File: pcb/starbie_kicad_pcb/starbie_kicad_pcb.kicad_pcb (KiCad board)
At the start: 2 copper layers, 7 parts, among them J1 Conn_01x04_Pin, J2 Conn_01x08_Pin, SW1 SW_Push, SW2 SW_Push, U1 DHT11, U2 XIAO-ESP32-C3-SMD

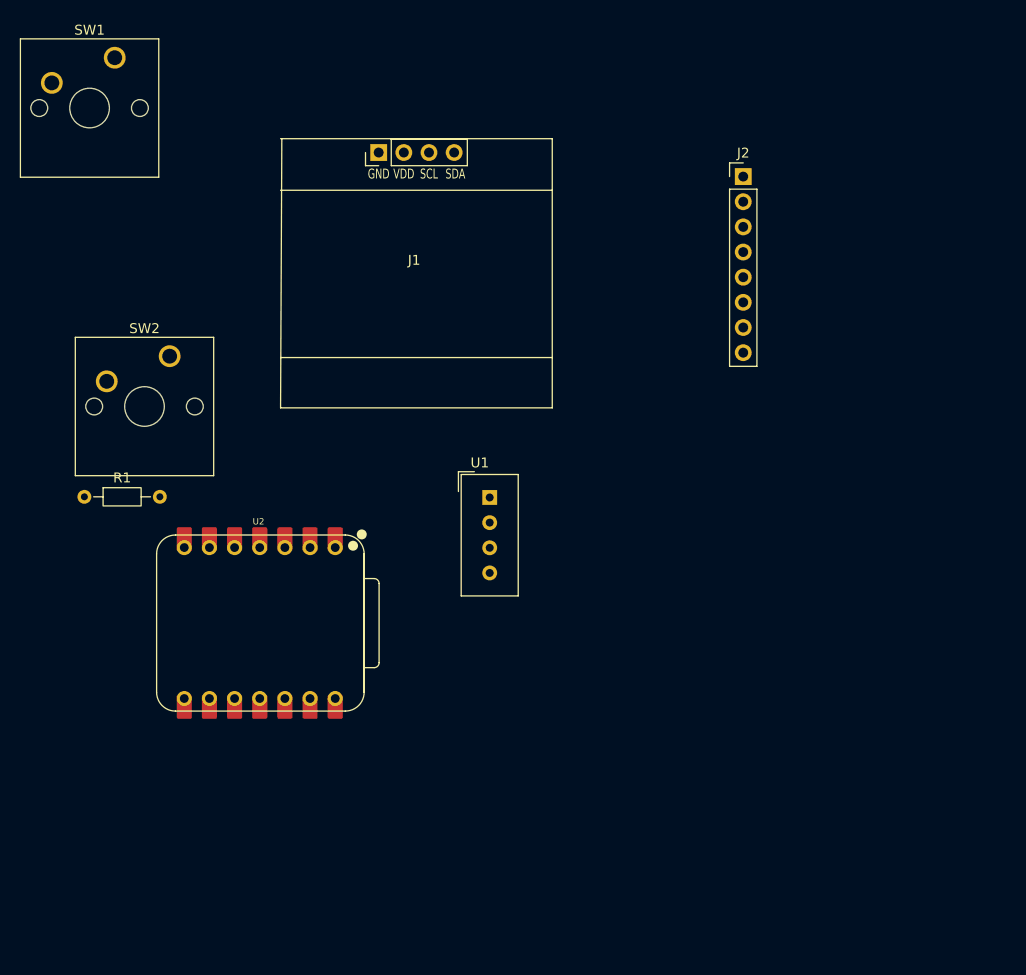
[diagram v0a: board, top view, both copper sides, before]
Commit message: added arduino sketch files
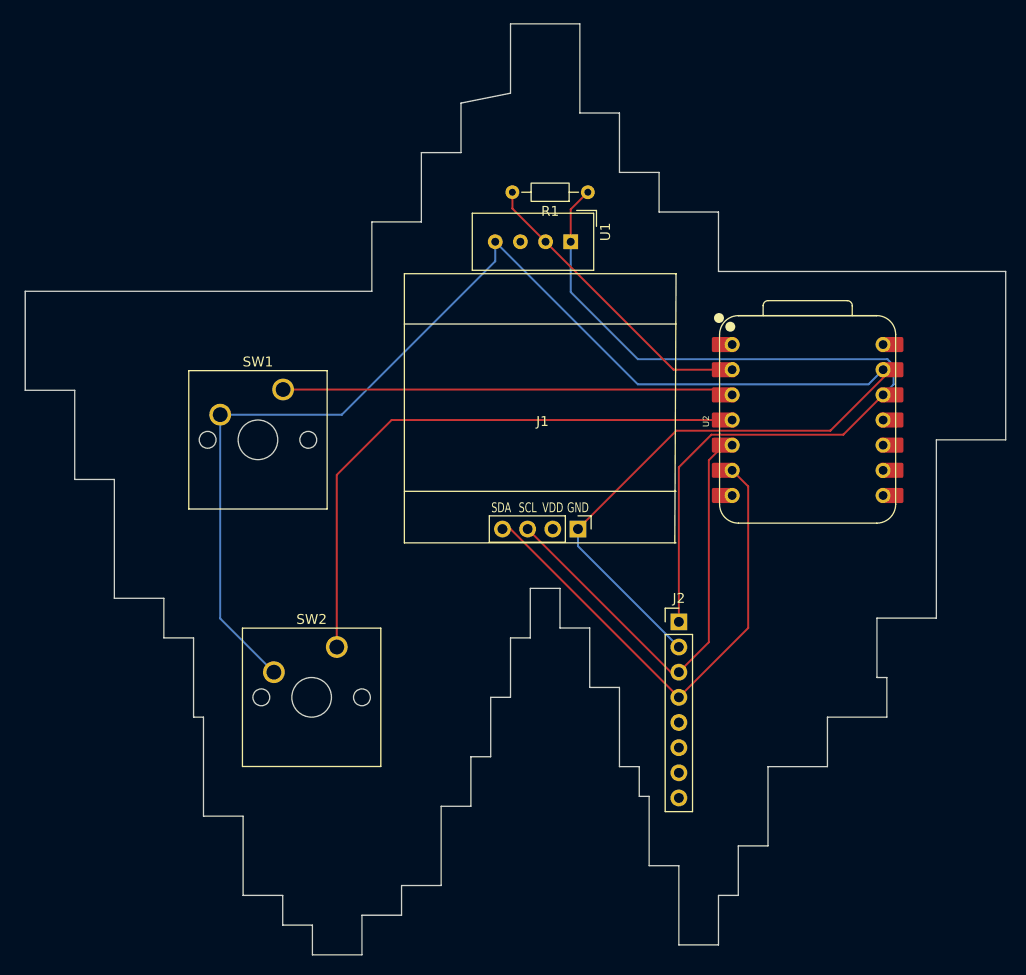
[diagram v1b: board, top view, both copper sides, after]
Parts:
- moved R1 59.4 mm to (152.8, 57.0), turned to 180 degrees
- moved U2 59.0 mm to (175.0, 80.0), turned to 90 degrees
- moved J2 45.4 mm to (162.0, 100.4)
- moved J1 40.0 mm to (148.0, 91.0), turned to 180 degrees
- moved SW1 37.6 mm to (122.0, 76.9)
- moved SW2 33.9 mm to (127.5, 102.9)
- moved U1 27.1 mm to (151.1, 62.0), turned to -90 degrees
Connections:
- J1 pad 1: unconnected-(J1-Pin_1-Pad1) -> GND
- J1 pad 2: unconnected-(J1-Pin_2-Pad2) -> +3.3V
- J1 pad 3: unconnected-(J1-Pin_3-Pad3) -> /SCL
- J1 pad 4: unconnected-(J1-Pin_4-Pad4) -> /SDA
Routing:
- net GND: track 0.00 -> 164.6 mm
- net +3.3V: track 0.00 -> 89.1 mm
- net /GPIO3: track 0.00 -> 59.6 mm
- net /SDA: track 0.00 -> 51.7 mm
- net /SCL: track 0.00 -> 46.1 mm
- net /GPIO2: track 0.00 -> 44.7 mm
- net /DHT11 DATA: track 0.00 -> 29.7 mm
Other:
- board outline added: 99 x 94 mm
